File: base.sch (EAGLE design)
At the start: 1 part, among them U1 XC7K160TFBG484

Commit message: adding DRAM.
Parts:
- added J1: AS0A626-U2SN-7F, AS0A626-U2SN-7F:AS0A626-U2SN-7F
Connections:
- removed net N$1: U1B13.VCCO_13@0, U1B13.VCCO_13@1, U1B13.VCCO_13@2, U1B13.VCCO_13@3, U1B13.VCCO_13@4, U1B13.VCCO_13@5
- removed net N$2: U1B0.VCCO_0@0
- removed net N$3: U1B0.VCCO_0@1
- removed net N$4: U1B14.VCCO_14@0, U1B14.VCCO_14@1, U1B14.VCCO_14@2, U1B14.VCCO_14@3, U1B14.VCCO_14@4, U1B14.VCCO_14@5
- removed net N$5: U1B15.VCCO_15@0, U1B15.VCCO_15@1, U1B15.VCCO_15@2, U1B15.VCCO_15@3, U1B15.VCCO_15@4, U1B15.VCCO_15@5
- removed net N$6: U1B16.VCCO_16@0, U1B16.VCCO_16@1, U1B16.VCCO_16@2, U1B16.VCCO_16@3
- removed net N$7: U1B33.VCCO_33@0, U1B33.VCCO_33@1, U1B33.VCCO_33@2, U1B33.VCCO_33@3, U1B33.VCCO_33@4, U1B33.VCCO_33@5
- removed net N$8: U1B34.VCCO_34@0, U1B34.VCCO_34@1, U1B34.VCCO_34@2, U1B34.VCCO_34@3, U1B34.VCCO_34@4, U1B34.VCCO_34@5
- new net VADJ_FPGA: U1B13.VCCO_13@0, U1B13.VCCO_13@1, U1B13.VCCO_13@2, U1B13.VCCO_13@3, U1B13.VCCO_13@4, U1B13.VCCO_13@5, U1B16.VCCO_16@0, U1B16.VCCO_16@1, U1B16.VCCO_16@2, U1B16.VCCO_16@3
- new net VCC1V5_FPGA: U1B33.VCCO_33@0, U1B33.VCCO_33@1, U1B33.VCCO_33@2, U1B33.VCCO_33@3, U1B33.VCCO_33@4, U1B33.VCCO_33@5, U1B34.VCCO_34@0, U1B34.VCCO_34@1, U1B34.VCCO_34@2, U1B34.VCCO_34@3, U1B34.VCCO_34@4, U1B34.VCCO_34@5
- net VCC2V5_FPGA: now also U1B0.VCCO_0@0, U1B0.VCCO_0@1, U1B14.VCCO_14@0, U1B14.VCCO_14@1, U1B14.VCCO_14@2, U1B14.VCCO_14@3, U1B14.VCCO_14@4, U1B14.VCCO_14@5, U1B15.VCCO_15@0, U1B15.VCCO_15@1, U1B15.VCCO_15@2, U1B15.VCCO_15@3, U1B15.VCCO_15@4, U1B15.VCCO_15@5

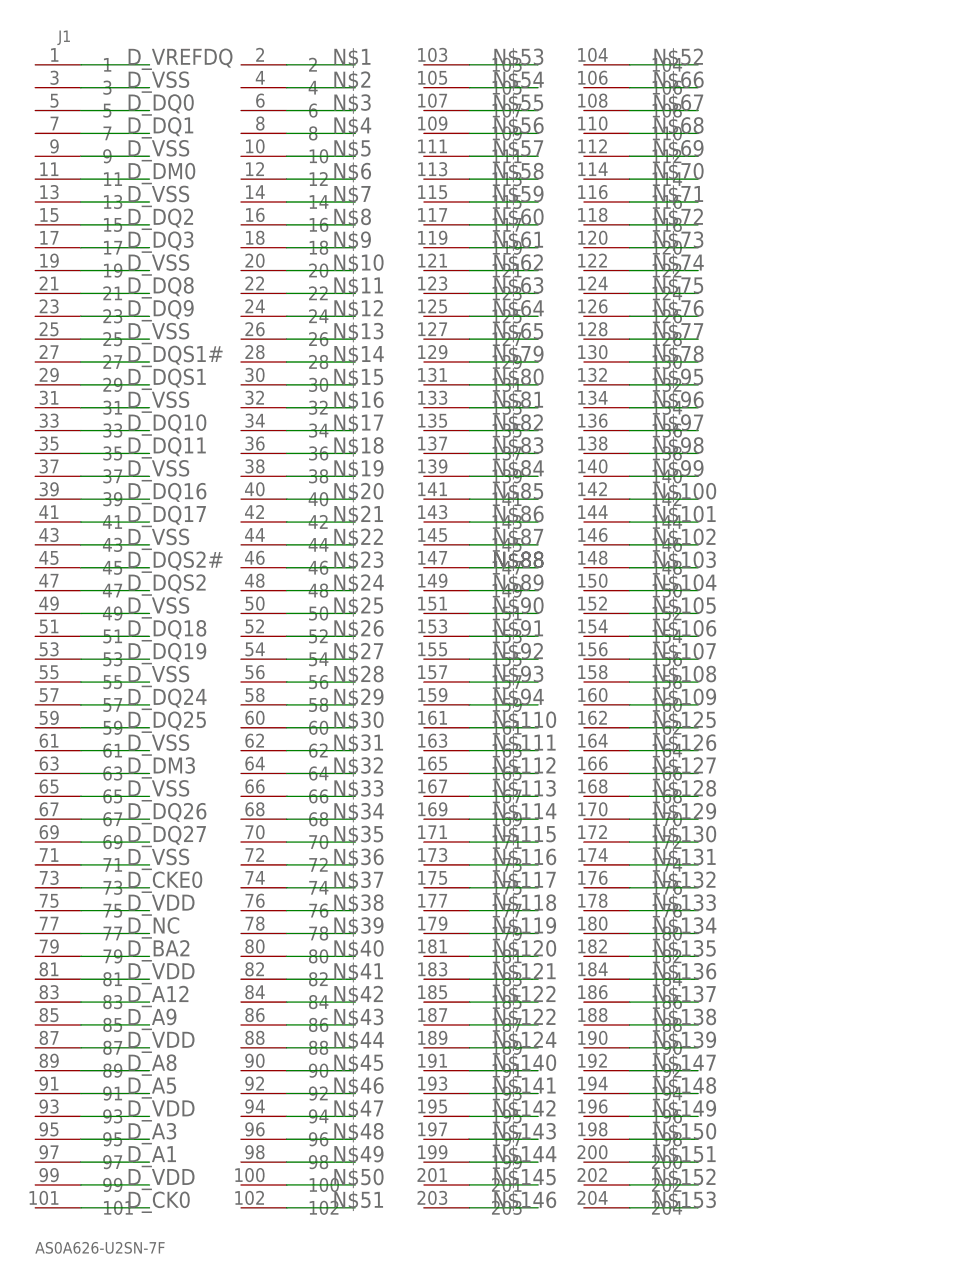
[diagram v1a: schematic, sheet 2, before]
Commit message: updates to DRAM.
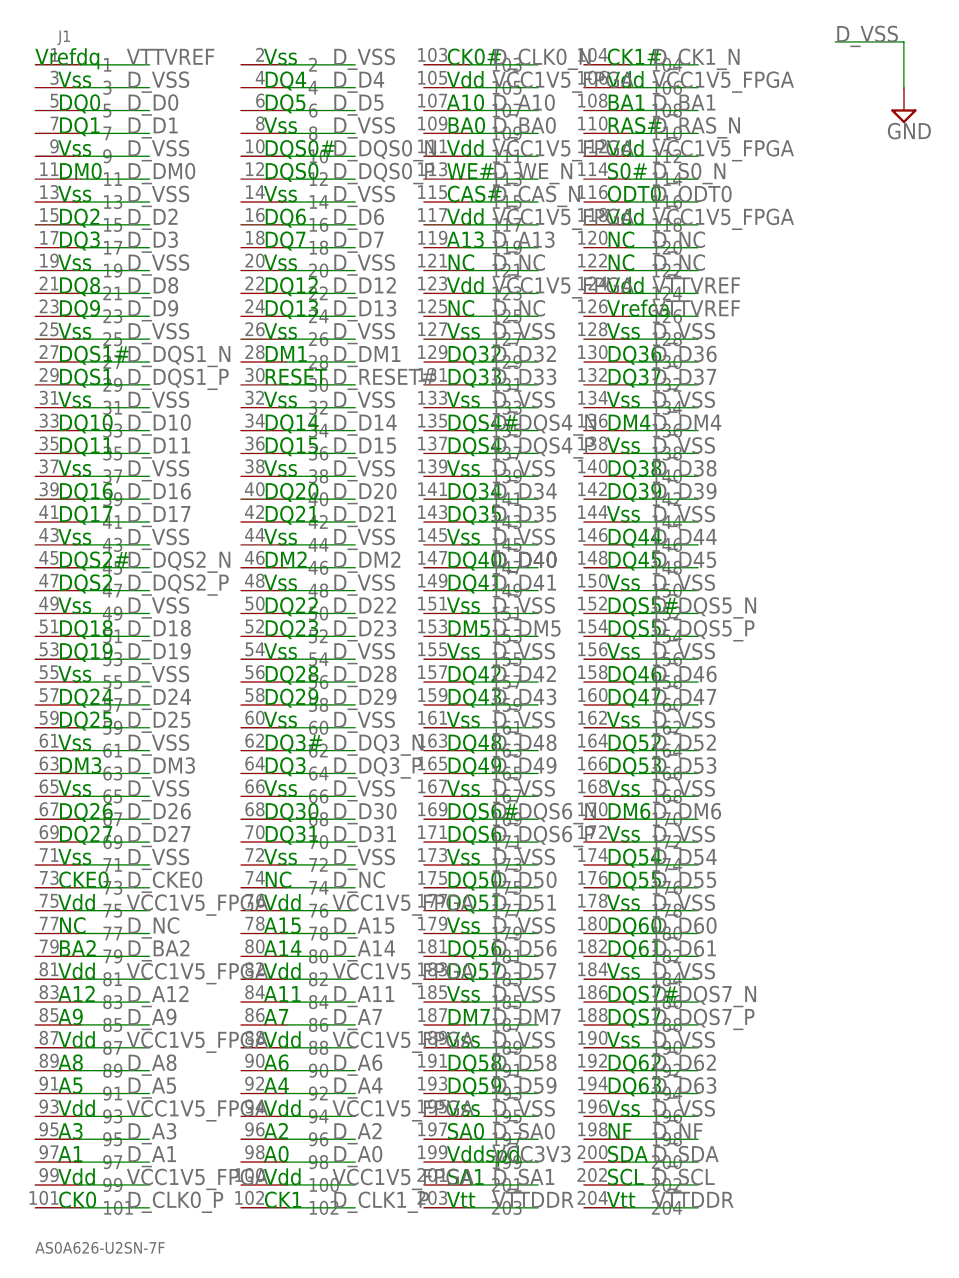
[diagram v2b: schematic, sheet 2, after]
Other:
- note added: "A0"
- note added: "A1"
- note added: "A10"
- note added: "A11"
- note added: "A12"
- note added: "A13"
- note added: "A14"
- note added: "A15"
- note added: "A2"
- note added: "A3"
- note added: "A4"
- note added: "A5"
- note added: "A6"
- note added: "A7"
- note added: "A8"
- note added: "A9"
- note added: "BA0"
- note added: "BA1"
- note added: "BA2"
- note added: "CAS#"
- note added: "CK0"
- note added: "CK0#"
- note added: "CK1"
- note added: "CK1#"
- note added: "CKE0"
- note added: "DM0"
- note added: "DM1"
- note added: "DM2"
- note added: "DM3"
- note added: "DM4"
- note added: "DM5"
- note added: "DM6"
- note added: "DM7"
- note added: "DQ0"
- note added: "DQ1"
- note added: "DQ10"
- note added: "DQ11"
- note added: "DQ12"
- note added: "DQ13"
- note added: "DQ14"
- note added: "DQ15"
- note added: "DQ16"
- note added: "DQ17"
- note added: "DQ18"
- note added: "DQ19"
- note added: "DQ2"
- note added: "DQ20"
- note added: "DQ21"
- note added: "DQ22"
- note added: "DQ23"
- note added: "DQ24"
- note added: "DQ25"
- note added: "DQ26"
- note added: "DQ27"
- note added: "DQ28"
- note added: "DQ29"
- note added: "DQ3"
- note added: "DQ3#"
- note added: "DQ30"
- note added: "DQ31"
- note added: "DQ32"
- note added: "DQ33"
- note added: "DQ34"
- note added: "DQ35"
- note added: "DQ36"
- note added: "DQ37"
- note added: "DQ38"
- note added: "DQ39"
- note added: "DQ4"
- note added: "DQ40"
- note added: "DQ41"
- note added: "DQ42"
- note added: "DQ43"
- note added: "DQ44"
- note added: "DQ45"
- note added: "DQ46"
- note added: "DQ47"
- note added: "DQ48"
- note added: "DQ49"
- note added: "DQ5"
- note added: "DQ50"
- note added: "DQ51"
- note added: "DQ52"
- note added: "DQ53"
- note added: "DQ54"
- note added: "DQ55"
- note added: "DQ56"
- note added: "DQ57"
- note added: "DQ58"
- note added: "DQ59"
- note added: "DQ6"
- note added: "DQ60"
- note added: "DQ61"
- note added: "DQ62"
- note added: "DQ63"
- note added: "DQ7"
- note added: "DQ8"
- note added: "DQ9"
- note added: "DQS0"
- note added: "DQS0#"
- note added: "DQS1"
- note added: "DQS1#"
- note added: "DQS2"
- note added: "DQS2#"
- note added: "DQS4"
- note added: "DQS4#"
- note added: "DQS5"
- note added: "DQS5#"
- note added: "DQS6"
- note added: "DQS6#"
- note added: "DQS7"
- note added: "DQS7#"
- note added: "NC"
- note added: "NF"
- note added: "ODT0"
- note added: "RAS#"
- note added: "RESET"
- note added: "S0#"
- note added: "SA0"
- note added: "SA1"
- note added: "SCL"
- note added: "SDA"
- note added: "Vdd"
- note added: "Vddspd"
- note added: "Vrefca"
- note added: "Vrefdq"
- note added: "Vss"
- note added: "Vtt"
- note added: "WE#"

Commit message: dram wired.
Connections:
- new net D_A0: J1.98, U1B13.IO_L23N_T3_13
- new net D_A1: J1.97, U1B13.IO_L24P_T3_13
- new net D_A10: J1.107, U1B16.IO_L11N_T1_SRCC_16
- new net D_A11: J1.84, U1B16.IO_L12P_T1_MRCC_16
- new net D_A12: J1.83, U1B16.IO_L12N_T1_MRCC_16
- new net D_A13: J1.119, U1B16.IO_L13P_T2_MRCC_16
- new net D_A14: J1.80, U1B16.IO_L13N_T2_MRCC_16
- new net D_A15: J1.78, U1B16.IO_L14P_T2_SRCC_16
- new net D_A2: J1.96, U1B13.IO_L24N_T3_13
- new net D_A3: J1.95, U1B16.IO_L7P_T1_16
- new net D_A4: J1.92, U1B16.IO_L7N_T1_16
- new net D_A5: J1.91, U1B16.IO_L8P_T1_16
- new net D_A6: J1.90, U1B16.IO_L8N_T1_16
- new net D_A7: J1.86, U1B16.IO_L10P_T1_16
- new net D_A8: J1.89, U1B16.IO_L10N_T1_16
- new net D_A9: J1.85, U1B16.IO_L11P_T1_SRCC_16
- new net D_BA0: J1.109, U1B16.IO_L14N_T2_SRCC_16
- new net D_BA1: J1.108, U1B16.IO_L16P_T2_16
- new net D_BA2: J1.79, U1B16.IO_L16N_T2_16
- new net D_CAS_N: J1.115, U1B16.IO_L23N_T3_16
- new net D_CKE0: J1.73, U1B16.IO_L17P_T2_16
- new net D_CLK0_N: J1.103, U1B16.IO_L19P_T3_16
- new net D_CLK0_P: J1.101, U1B16.IO_L20P_T3_16
- new net D_CLK1_N: J1.104, U1B16.IO_L20N_T3_16
- new net D_CLK1_P: J1.102, U1B16.IO_L22P_T3_16
- new net D_D0: J1.5, U1B13.IO_L5N_T0_13
- new net D_D1: J1.7, U1B13.IO_L2P_T0_13
- new net D_D10: J1.33, U1B13.IO_L7N_T1_13
- new net D_D11: J1.35, U1B13.IO_L11P_T1_SRCC_13
- new net D_D12: J1.22, U1B13.IO_L10P_T1_13
- new net D_D13: J1.24, U1B13.IO_L8N_T1_13
- new net D_D14: J1.34, U1B13.IO_L11N_T1_SRCC_13
- new net D_D15: J1.36, U1B33.IO_L15P_T2_DQS_33
- new net D_D16: J1.39, U1B13.IO_L16P_T2_13
- new net D_D17: J1.41, U1B13.IO_L16N_T2_13
- new net D_D18: J1.51, U1B13.IO_L12N_T1_MRCC_13
- new net D_D19: J1.53, U1B13.IO_L13P_T2_MRCC_13
- new net D_D2: J1.15, U1B13.IO_L4N_T0_13
- new net D_D20: J1.40, U1B13.IO_L14N_T2_SRCC_13
- new net D_D21: J1.42, U1B13.IO_L17P_T2_13
- new net D_D22: J1.50, U1B13.IO_L13N_T2_MRCC_13
- new net D_D23: J1.52, U1B13.IO_L14P_T2_SRCC_13
- new net D_D24: J1.57, U1B13.IO_L23P_T3_13
- new net D_D25: J1.59, U1B13.IO_L18P_T2_13
- new net D_D26: J1.67, U1B13.IO_L22P_T3_13
- new net D_D27: J1.69, U1B13.IO_L20P_T3_13
- new net D_D28: J1.56, U1B13.IO_L18N_T2_13
- new net D_D29: J1.58, U1B13.IO_L19P_T3_13
- new net D_D3: J1.17, U1B13.IO_L4P_T0_13
- new net D_D30: J1.68, U1B13.IO_L20N_T3_13
- new net D_D31: J1.70, U1B13.IO_L22N_T3_13
- new net D_D32: J1.129, U1B33.IO_L5P_T0_33
- new net D_D33: J1.131, U1B33.IO_L6P_T0_33
- new net D_D34: J1.141, U1B33.IO_L7N_T1_33
- new net D_D35: J1.143, U1B33.IO_L8P_T1_33
- new net D_D36: J1.130, U1B33.IO_L8N_T1_33
- new net D_D37: J1.132, U1B33.IO_L4P_T0_33
- new net D_D38: J1.140, U1B33.IO_L5N_T0_33
- new net D_D39: J1.142, U1B33.IO_L7P_T1_33
- new net D_D4: J1.4, U1B13.IO_L2N_T0_13
- new net D_D40: J1.147, U1B33.IO_L12N_T1_MRCC_33
- new net D_D41: J1.149, U1B33.IO_L13P_T2_MRCC_33
- new net D_D42: J1.157, U1B33.IO_L11N_T1_SRCC_33
- new net D_D43: J1.159, U1B33.IO_L12P_T1_MRCC_33
- new net D_D44: J1.146, U1B33.IO_L14P_T2_SRCC_33
- new net D_D45: J1.148, U1B33.IO_L13N_T2_MRCC_33
- new net D_D46: J1.158, U1B33.IO_L10N_T1_33
- new net D_D47: J1.160, U1B33.IO_L11P_T1_SRCC_33
- new net D_D48: J1.163, U1B33.IO_L18P_T2_33
- new net D_D49: J1.165, U1B33.IO_L19P_T3_33
- new net D_D5: J1.6, U1B13.IO_L5P_T0_13
- new net D_D50: J1.175, U1B33.IO_L17N_T2_33
- new net D_D51: J1.177, U1B33.IO_L17P_T2_33
- new net D_D52: J1.164, U1B33.IO_L20P_T3_33
- new net D_D53: J1.166, U1B33.IO_L16P_T2_33
- new net D_D54: J1.174, U1B33.IO_L18N_T2_33
- new net D_D55: J1.176, U1B33.IO_L16N_T2_33
- new net D_D56: J1.181, U1B33.IO_L24P_T3_33
- new net D_D57: J1.183, U1B33.IO_L9P_T1_DQS_33
- new net D_D58: J1.191, U1B33.IO_L23P_T3_33
- new net D_D59: J1.193, U1B33.IO_L23N_T3_33
- new net D_D6: J1.16, U1B13.IO_L6P_T0_13
- new net D_D60: J1.180, U1B33.IO_L22P_T3_33
- new net D_D61: J1.182, U1B33.IO_L22N_T3_33
- new net D_D62: J1.192, U1B33.IO_L24N_T3_33
- new net D_D63: J1.194, U1B33.IO_L9N_T1_DQS_33
- new net D_D7: J1.18, U1B13.IO_L1P_T0_13
- new net D_D8: J1.21, U1B13.IO_L8P_T1_13
- new net D_D9: J1.23, U1B13.IO_L10N_T1_13
- new net D_DM0: J1.11, U1B13.IO_L1N_T0_13
- new net D_DM1: J1.28, U1B13.IO_L7P_T1_13
- new net D_DM2: J1.46, U1B13.IO_L12P_T1_MRCC_13
- new net D_DM3: J1.63, U1B13.IO_L17N_T2_13
- new net D_DM4: J1.136, U1B33.IO_L4N_T0_33
- new net D_DM5: J1.153, U1B33.IO_L10P_T1_33
- new net D_DM6: J1.170, U1B33.IO_L14N_T2_SRCC_33
- new net D_DM7: J1.187, U1B33.IO_L20N_T3_33
- new net D_DQS0_N: J1.10, U1B13.IO_L3N_T0_DQS_13
- new net D_DQS0_P: J1.12, U1B13.IO_L3P_T0_DQS_13
- new net D_DQS1_N: J1.27, U1B13.IO_L9N_T1_DQS_13
- new net D_DQS1_P: J1.29, U1B13.IO_L9P_T1_DQS_13
- new net D_DQS2_N: J1.45, U1B13.IO_L15N_T2_DQS_13
- new net D_DQS2_P: J1.47, U1B13.IO_L15P_T2_DQS_13
- new net D_DQS3_N: J1.62, U1B13.IO_L21N_T3_DQS_13
- new net D_DQS3_P: J1.64, U1B13.IO_L21P_T3_DQS_13
- new net D_DQS4_N: J1.135, U1B16.IO_L9N_T1_DQS_16
- new net D_DQS4_P: J1.137, U1B16.IO_L9P_T1_DQS_16
- new net D_DQS5_N: J1.152, U1B16.IO_L15N_T2_DQS_16
- new net D_DQS5_P: J1.154, U1B16.IO_L15P_T2_DQS_16
- new net D_DQS6_N: J1.169, U1B16.IO_L21N_T3_DQS_16
- new net D_DQS6_P: J1.171, U1B16.IO_L21P_T3_DQS_16
- new net D_DQS7_N: J1.186, U1B33.IO_L3P_T0_DQS_33
- new net D_DQS7_P: J1.188, U1B33.IO_L3N_T0_DQS_33
- new net D_NC: J1.120, J1.121, J1.122, J1.125, J1.74, J1.77
- new net D_ODT0: J1.116, U1B33.IO_L2P_T0_33
- new net D_RAS_N: J1.110, U1B16.IO_L23P_T3_16
- new net D_RESET_N: J1.30, U1B33.IO_L15N_T2_DQS_33
- new net D_S0_N: J1.114, U1B33.IO_L1P_T0_33
- new net D_SCL: J1.202
- new net D_SDA: J1.200
- new net D_VSS: J1.127, J1.128, J1.13, J1.133, J1.134, J1.138, J1.139, J1.14, J1.144, J1.145, J1.150, J1.151, J1.155, J1.156, J1.161, J1.162, J1.167, J1.168, J1.172, J1.173, J1.178, J1.179, J1.184, J1.185, J1.189, J1.19, J1.190, J1.195, J1.196, J1.2, J1.20, J1.25, J1.26, J1.3, J1.31, J1.32, J1.37, J1.38, J1.43, J1.44, J1.48, J1.49, J1.54, J1.55, J1.60, J1.61, J1.65, J1.66, J1.71, J1.72, J1.8, J1.9
- new net D_WE_N: J1.113, U1B16.IO_L22N_T3_16
- new net VCC3V3: J1.199
- new net VTTDDR: J1.203, J1.204
- new net VTTVREF: J1.1, J1.124, J1.126, U1B13.IO_L19N_T3_VREF_13, U1B13.IO_L6N_T0_VREF_13, U1B14.IO_L19N_T3_A09_D25_VREF_14, U1B14.IO_L6N_T0_D08_VREF_14, U1B15.IO_L19N_T3_A21_VREF_15, U1B15.IO_L6N_T0_VREF_15, U1B16.IO_6_T0_VREF_16, U1B16.IO_L19N_T3_VREF_16, U1B33.IO_L19N_T3_VREF_33, U1B33.IO_L6N_T0_VREF_33, U1B34.IO_L19N_T3_VREF_34, U1B34.IO_L6N_T0_VREF_34
- net GND: now also J1.197, J1.198, J1.201
- net VCC1V5_FPGA: now also J1.100, J1.105, J1.106, J1.111, J1.112, J1.117, J1.118, J1.123, J1.75, J1.76, J1.81, J1.82, J1.87, J1.88, J1.93, J1.94, J1.99

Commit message: reverting dram, bigger chip.
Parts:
- removed U1: XC7K160TFBG484, xilinx_devices_V6:XC7K160TFBG484
- added U2: XC7K160TFBG676, xilinx_devices_V6:XC7K160TFBG676
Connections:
- removed net FPGA_CCLK: U1B0.CCLK_0
- removed net FPGA_DONE: U1B0.DONE_0
- removed net FPGA_INIT_B: U1B0.INIT_B_0
- removed net FPGA_M0: U1B0.M0_0
- removed net FPGA_M1: U1B0.M1_0
- removed net FPGA_M2: U1B0.M2_0
- removed net FPGA_PROG_B: U1B0.PROGRAM_B_0
- removed net FPGA_TCK_BUF: U1B0.TCK_0
- removed net FPGA_TDI_BUF: U1B0.TDI_0
- removed net FPGA_TMS_BUF: U1B0.TMS_0
- removed net FPGA_VBATT: U1B0.VCCBATT_0
- removed net JTAG_TDO: U1B0.TDO_0
- removed net MGTAVCC: U1BMGTAVCC.MGTAVCC@0, U1BMGTAVCC.MGTAVCC@1, U1BMGTAVCC.MGTAVCC@2, U1BMGTAVCC.MGTAVCC@3
- removed net MGTAVTT: U1BMGTAVTT.MGTAVTT@0, U1BMGTAVTT.MGTAVTT@1, U1BMGTAVTT.MGTAVTT@2, U1BMGTAVTT.MGTAVTT@3
- removed net MGTVCCAUX: U1BMGTVCCAUX.MGTVCCAUX
- removed net VADJ_FPGA: U1B13.VCCO_13@0, U1B13.VCCO_13@1, U1B13.VCCO_13@2, U1B13.VCCO_13@3, U1B13.VCCO_13@4, U1B13.VCCO_13@5, U1B16.VCCO_16@0, U1B16.VCCO_16@1, U1B16.VCCO_16@2, U1B16.VCCO_16@3
- removed net VCC2V5_FPGA: U1B0.CFGBVS_0, U1B0.VCCO_0@0, U1B0.VCCO_0@1, U1B14.VCCO_14@0, U1B14.VCCO_14@1, U1B14.VCCO_14@2, U1B14.VCCO_14@3, U1B14.VCCO_14@4, U1B14.VCCO_14@5, U1B15.VCCO_15@0, U1B15.VCCO_15@1, U1B15.VCCO_15@2, U1B15.VCCO_15@3, U1B15.VCCO_15@4, U1B15.VCCO_15@5
- removed net VCCINT_FPGA: U1BVCCINT.VCCINT@0, U1BVCCINT.VCCINT@1, U1BVCCINT.VCCINT@10, U1BVCCINT.VCCINT@11, U1BVCCINT.VCCINT@12, U1BVCCINT.VCCINT@13, U1BVCCINT.VCCINT@2, U1BVCCINT.VCCINT@3, U1BVCCINT.VCCINT@4, U1BVCCINT.VCCINT@5, U1BVCCINT.VCCINT@6, U1BVCCINT.VCCINT@7, U1BVCCINT.VCCINT@8, U1BVCCINT.VCCINT@9
- removed net VCC_AUX: U1BVCCAUX.VCCAUX@0, U1BVCCAUX.VCCAUX@1, U1BVCCAUX.VCCAUX@2, U1BVCCAUX.VCCAUX@3, U1BVCCAUX.VCCAUX@4, U1BVCCAUX.VCCAUX@5, U1BVCCAUX.VCCAUX@6
- removed net VCC_BRAM: U1BVCCBRAM.VCCBRAM@0, U1BVCCBRAM.VCCBRAM@1, U1BVCCBRAM.VCCBRAM@2
- removed net XADC_AGND: U1BXADC.GNDADC_0, U1BXADC.VREFN_0
- removed net XADC_DXN: U1BTDIODE.DXN_0
- removed net XADC_DXP: U1BTDIODE.DXP_0
- removed net XADC_VCC: U1BXADC.VCCADC_0
- removed net XADC_VN_R: U1BXADC.VN_0
- removed net XADC_VP_R: U1BXADC.VP_0
- removed net XADC_VREFP: U1BXADC.VREFP_0
- new net F_CCLK: U2B0.CCLK_0
- new net F_DONE: U2B0.DONE_0
- new net F_INIT_N: U2B0.INIT_B_0
- new net F_M0: U2B0.M0_0
- new net F_M1: U2B0.M1_0
- new net F_M2: U2B0.M2_0
- new net F_PROG_N: U2B0.PROGRAM_B_0
- new net F_TCK_BUF: U2B0.TCK_0
- new net F_TDI_BUF: U2B0.TDI_0
- new net F_TDO: U2B0.TDO_0
- new net F_TMS_BUF: U2B0.TMS_0
- new net F_VBATT: U2B0.VCCBATT_0
- new net VADJ_F: U2B12.VCCO_12@0, U2B12.VCCO_12@1, U2B12.VCCO_12@2, U2B12.VCCO_12@3, U2B12.VCCO_12@4, U2B12.VCCO_12@5, U2B12.VCCO_12@6, U2B13.VCCO_13@0, U2B13.VCCO_13@1, U2B13.VCCO_13@2, U2B13.VCCO_13@3, U2B13.VCCO_13@4, U2B13.VCCO_13@5, U2B16.VCCO_16@0, U2B16.VCCO_16@1, U2B16.VCCO_16@2, U2B16.VCCO_16@3, U2B16.VCCO_16@4, U2B16.VCCO_16@5, U2B16.VCCO_16@6
- new net VCC1V5_F: U2B32.VCCO_32@0, U2B32.VCCO_32@1, U2B32.VCCO_32@2, U2B32.VCCO_32@3, U2B32.VCCO_32@4, U2B32.VCCO_32@5, U2B33.VCCO_33@0, U2B33.VCCO_33@1, U2B33.VCCO_33@2, U2B33.VCCO_33@3, U2B33.VCCO_33@4, U2B33.VCCO_33@5, U2B34.VCCO_34@0, U2B34.VCCO_34@1, U2B34.VCCO_34@2, U2B34.VCCO_34@3, U2B34.VCCO_34@4, U2B34.VCCO_34@5
- new net VCC2V5_F: U2B0.CFGBVS_0, U2B0.VCCO_0@0, U2B0.VCCO_0@1, U2B14.VCCO_14@0, U2B14.VCCO_14@1, U2B14.VCCO_14@2, U2B14.VCCO_14@3, U2B14.VCCO_14@4, U2B14.VCCO_14@5, U2B15.VCCO_15@0, U2B15.VCCO_15@1, U2B15.VCCO_15@2, U2B15.VCCO_15@3, U2B15.VCCO_15@4, U2B15.VCCO_15@5
- net D_A0: no longer U1B13.IO_L23N_T3_13
- net D_A1: no longer U1B13.IO_L24P_T3_13
- net D_A10: no longer U1B16.IO_L11N_T1_SRCC_16
- net D_A11: no longer U1B16.IO_L12P_T1_MRCC_16
- net D_A12: no longer U1B16.IO_L12N_T1_MRCC_16
- net D_A13: no longer U1B16.IO_L13P_T2_MRCC_16
- net D_A14: no longer U1B16.IO_L13N_T2_MRCC_16
- net D_A15: no longer U1B16.IO_L14P_T2_SRCC_16
- net D_A2: no longer U1B13.IO_L24N_T3_13
- net D_A3: no longer U1B16.IO_L7P_T1_16
- net D_A4: no longer U1B16.IO_L7N_T1_16
- net D_A5: no longer U1B16.IO_L8P_T1_16
- net D_A6: no longer U1B16.IO_L8N_T1_16
- net D_A7: no longer U1B16.IO_L10P_T1_16
- net D_A8: no longer U1B16.IO_L10N_T1_16
- net D_A9: no longer U1B16.IO_L11P_T1_SRCC_16
- net D_BA0: no longer U1B16.IO_L14N_T2_SRCC_16
- net D_BA1: no longer U1B16.IO_L16P_T2_16
- net D_BA2: no longer U1B16.IO_L16N_T2_16
- net D_CAS_N: no longer U1B16.IO_L23N_T3_16
- net D_CKE0: no longer U1B16.IO_L17P_T2_16
- net D_CLK0_N: no longer U1B16.IO_L19P_T3_16
- net D_CLK0_P: no longer U1B16.IO_L20P_T3_16
- net D_CLK1_N: no longer U1B16.IO_L20N_T3_16
- net D_CLK1_P: no longer U1B16.IO_L22P_T3_16
- net D_D0: no longer U1B13.IO_L5N_T0_13
- net D_D1: no longer U1B13.IO_L2P_T0_13
- net D_D10: no longer U1B13.IO_L7N_T1_13
- net D_D11: no longer U1B13.IO_L11P_T1_SRCC_13
- net D_D12: no longer U1B13.IO_L10P_T1_13
- net D_D13: no longer U1B13.IO_L8N_T1_13
- net D_D14: no longer U1B13.IO_L11N_T1_SRCC_13
- net D_D15: no longer U1B33.IO_L15P_T2_DQS_33
- net D_D16: no longer U1B13.IO_L16P_T2_13
- net D_D17: no longer U1B13.IO_L16N_T2_13
- net D_D18: no longer U1B13.IO_L12N_T1_MRCC_13
- net D_D19: no longer U1B13.IO_L13P_T2_MRCC_13
- net D_D2: no longer U1B13.IO_L4N_T0_13
- net D_D20: no longer U1B13.IO_L14N_T2_SRCC_13
- net D_D21: no longer U1B13.IO_L17P_T2_13
- net D_D22: no longer U1B13.IO_L13N_T2_MRCC_13
- net D_D23: no longer U1B13.IO_L14P_T2_SRCC_13
- net D_D24: no longer U1B13.IO_L23P_T3_13
- net D_D25: no longer U1B13.IO_L18P_T2_13
- net D_D26: no longer U1B13.IO_L22P_T3_13
- net D_D27: no longer U1B13.IO_L20P_T3_13
- net D_D28: no longer U1B13.IO_L18N_T2_13
- net D_D29: no longer U1B13.IO_L19P_T3_13
- net D_D3: no longer U1B13.IO_L4P_T0_13
- net D_D30: no longer U1B13.IO_L20N_T3_13
- net D_D31: no longer U1B13.IO_L22N_T3_13
- net D_D32: no longer U1B33.IO_L5P_T0_33
- net D_D33: no longer U1B33.IO_L6P_T0_33
- net D_D34: no longer U1B33.IO_L7N_T1_33
- net D_D35: no longer U1B33.IO_L8P_T1_33
- net D_D36: no longer U1B33.IO_L8N_T1_33
- net D_D37: no longer U1B33.IO_L4P_T0_33
- net D_D38: no longer U1B33.IO_L5N_T0_33
- net D_D39: no longer U1B33.IO_L7P_T1_33
- net D_D4: no longer U1B13.IO_L2N_T0_13
- net D_D40: no longer U1B33.IO_L12N_T1_MRCC_33
- net D_D41: no longer U1B33.IO_L13P_T2_MRCC_33
- net D_D42: no longer U1B33.IO_L11N_T1_SRCC_33
- net D_D43: no longer U1B33.IO_L12P_T1_MRCC_33
- net D_D44: no longer U1B33.IO_L14P_T2_SRCC_33
- net D_D45: no longer U1B33.IO_L13N_T2_MRCC_33
- net D_D46: no longer U1B33.IO_L10N_T1_33
- net D_D47: no longer U1B33.IO_L11P_T1_SRCC_33
- net D_D48: no longer U1B33.IO_L18P_T2_33
- net D_D49: no longer U1B33.IO_L19P_T3_33
- net D_D5: no longer U1B13.IO_L5P_T0_13
- net D_D50: no longer U1B33.IO_L17N_T2_33
- net D_D51: no longer U1B33.IO_L17P_T2_33
- net D_D52: no longer U1B33.IO_L20P_T3_33
- net D_D53: no longer U1B33.IO_L16P_T2_33
- net D_D54: no longer U1B33.IO_L18N_T2_33
- net D_D55: no longer U1B33.IO_L16N_T2_33
- net D_D56: no longer U1B33.IO_L24P_T3_33
- net D_D57: no longer U1B33.IO_L9P_T1_DQS_33
- net D_D58: no longer U1B33.IO_L23P_T3_33
- net D_D59: no longer U1B33.IO_L23N_T3_33
- net D_D6: no longer U1B13.IO_L6P_T0_13
- net D_D60: no longer U1B33.IO_L22P_T3_33
- net D_D61: no longer U1B33.IO_L22N_T3_33
- net D_D62: no longer U1B33.IO_L24N_T3_33
- net D_D63: no longer U1B33.IO_L9N_T1_DQS_33
- net D_D7: no longer U1B13.IO_L1P_T0_13
- net D_D8: no longer U1B13.IO_L8P_T1_13
- net D_D9: no longer U1B13.IO_L10N_T1_13
- net D_DM0: no longer U1B13.IO_L1N_T0_13
- net D_DM1: no longer U1B13.IO_L7P_T1_13
- net D_DM2: no longer U1B13.IO_L12P_T1_MRCC_13
- net D_DM3: no longer U1B13.IO_L17N_T2_13
- net D_DM4: no longer U1B33.IO_L4N_T0_33
- net D_DM5: no longer U1B33.IO_L10P_T1_33
- net D_DM6: no longer U1B33.IO_L14N_T2_SRCC_33
- net D_DM7: no longer U1B33.IO_L20N_T3_33
- net D_DQS0_N: no longer U1B13.IO_L3N_T0_DQS_13
- net D_DQS0_P: no longer U1B13.IO_L3P_T0_DQS_13
- net D_DQS1_N: no longer U1B13.IO_L9N_T1_DQS_13
- net D_DQS1_P: no longer U1B13.IO_L9P_T1_DQS_13
- net D_DQS2_N: no longer U1B13.IO_L15N_T2_DQS_13
- net D_DQS2_P: no longer U1B13.IO_L15P_T2_DQS_13
- net D_DQS3_N: no longer U1B13.IO_L21N_T3_DQS_13
- net D_DQS3_P: no longer U1B13.IO_L21P_T3_DQS_13
- net D_DQS4_N: no longer U1B16.IO_L9N_T1_DQS_16
- net D_DQS4_P: no longer U1B16.IO_L9P_T1_DQS_16
- net D_DQS5_N: no longer U1B16.IO_L15N_T2_DQS_16
- net D_DQS5_P: no longer U1B16.IO_L15P_T2_DQS_16
- net D_DQS6_N: no longer U1B16.IO_L21N_T3_DQS_16
- net D_DQS6_P: no longer U1B16.IO_L21P_T3_DQS_16
- net D_DQS7_N: no longer U1B33.IO_L3P_T0_DQS_33
- net D_DQS7_P: no longer U1B33.IO_L3N_T0_DQS_33
- net D_ODT0: no longer U1B33.IO_L2P_T0_33
- net D_RAS_N: no longer U1B16.IO_L23P_T3_16
- net D_RESET_N: no longer U1B33.IO_L15N_T2_DQS_33
- net D_S0_N: no longer U1B33.IO_L1P_T0_33
- net D_WE_N: no longer U1B16.IO_L22N_T3_16
- net GND: now also U2BGNDA.GND@0, U2BGNDA.GND@1, U2BGNDA.GND@10, U2BGNDA.GND@11, U2BGNDA.GND@12, U2BGNDA.GND@13, U2BGNDA.GND@14, U2BGNDA.GND@15, U2BGNDA.GND@16, U2BGNDA.GND@17, U2BGNDA.GND@18, U2BGNDA.GND@19, U2BGNDA.GND@2, U2BGNDA.GND@20, U2BGNDA.GND@21, U2BGNDA.GND@22, U2BGNDA.GND@23, U2BGNDA.GND@24, U2BGNDA.GND@25, U2BGNDA.GND@26, U2BGNDA.GND@27, U2BGNDA.GND@28, U2BGNDA.GND@29, U2BGNDA.GND@3, U2BGNDA.GND@30, U2BGNDA.GND@31, U2BGNDA.GND@32, U2BGNDA.GND@33, U2BGNDA.GND@34, U2BGNDA.GND@35, U2BGNDA.GND@36, U2BGNDA.GND@37, U2BGNDA.GND@38, U2BGNDA.GND@39, U2BGNDA.GND@4, U2BGNDA.GND@5, U2BGNDA.GND@6, U2BGNDA.GND@7, U2BGNDA.GND@8, U2BGNDA.GND@9, U2BGNDB.GND@40, U2BGNDB.GND@41, U2BGNDB.GND@42, U2BGNDB.GND@43, U2BGNDB.GND@44, U2BGNDB.GND@45, U2BGNDB.GND@46, U2BGNDB.GND@47, U2BGNDB.GND@48, U2BGNDB.GND@49, U2BGNDB.GND@50, U2BGNDB.GND@51, U2BGNDB.GND@52, U2BGNDB.GND@53, U2BGNDB.GND@54, U2BGNDB.GND@55, U2BGNDB.GND@56, U2BGNDB.GND@57, U2BGNDB.GND@58, U2BGNDB.GND@59, U2BGNDB.GND@60, U2BGNDB.GND@61, U2BGNDB.GND@62, U2BGNDB.GND@63, U2BGNDB.GND@64, U2BGNDB.GND@65, U2BGNDB.GND@66, U2BGNDB.GND@67, U2BGNDB.GND@68, U2BGNDB.GND@69, U2BGNDB.GND@70, U2BGNDB.GND@71, U2BGNDB.GND@72, U2BGNDB.GND@73, U2BGNDB.GND@74, U2BGNDB.GND@75, U2BGNDB.GND@76, U2BGNDB.GND@77, U2BGNDB.GND@78, U2BGNDB.GND@79, U2BGNDC.GND@100, U2BGNDC.GND@101, U2BGNDC.GND@102, U2BGNDC.GND@103, U2BGNDC.GND@104, U2BGNDC.GND@105, U2BGNDC.GND@106, U2BGNDC.GND@107, U2BGNDC.GND@108, U2BGNDC.GND@109, U2BGNDC.GND@110, U2BGNDC.GND@111, U2BGNDC.GND@112, U2BGNDC.GND@113, U2BGNDC.GND@114, U2BGNDC.GND@115, U2BGNDC.GND@116, U2BGNDC.GND@117, U2BGNDC.GND@118, U2BGNDC.GND@119, U2BGNDC.GND@80, U2BGNDC.GND@81, U2BGNDC.GND@82, U2BGNDC.GND@83, U2BGNDC.GND@84, U2BGNDC.GND@85, U2BGNDC.GND@86, U2BGNDC.GND@87, U2BGNDC.GND@88, U2BGNDC.GND@89, U2BGNDC.GND@90, U2BGNDC.GND@91, U2BGNDC.GND@92, U2BGNDC.GND@93, U2BGNDC.GND@94, U2BGNDC.GND@95, U2BGNDC.GND@96, U2BGNDC.GND@97, U2BGNDC.GND@98, U2BGNDC.GND@99; no longer U1BGNDA.GND@0, U1BGNDA.GND@1, U1BGNDA.GND@10, U1BGNDA.GND@11, U1BGNDA.GND@12, U1BGNDA.GND@13, U1BGNDA.GND@14, U1BGNDA.GND@15, U1BGNDA.GND@16, U1BGNDA.GND@17, U1BGNDA.GND@18, U1BGNDA.GND@19, U1BGNDA.GND@2, U1BGNDA.GND@20, U1BGNDA.GND@21, U1BGNDA.GND@22, U1BGNDA.GND@23, U1BGNDA.GND@24, U1BGNDA.GND@25, U1BGNDA.GND@26, U1BGNDA.GND@27, U1BGNDA.GND@28, U1BGNDA.GND@29, U1BGNDA.GND@3, U1BGNDA.GND@30, U1BGNDA.GND@31, U1BGNDA.GND@32, U1BGNDA.GND@33, U1BGNDA.GND@34, U1BGNDA.GND@35, U1BGNDA.GND@36, U1BGNDA.GND@37, U1BGNDA.GND@38, U1BGNDA.GND@39, U1BGNDA.GND@4, U1BGNDA.GND@40, U1BGNDA.GND@41, U1BGNDA.GND@42, U1BGNDA.GND@43, U1BGNDA.GND@5, U1BGNDA.GND@6, U1BGNDA.GND@7, U1BGNDA.GND@8, U1BGNDA.GND@9, U1BGNDB.GND@44, U1BGNDB.GND@45, U1BGNDB.GND@46, U1BGNDB.GND@47, U1BGNDB.GND@48, U1BGNDB.GND@49, U1BGNDB.GND@50, U1BGNDB.GND@51, U1BGNDB.GND@52, U1BGNDB.GND@53, U1BGNDB.GND@54, U1BGNDB.GND@55, U1BGNDB.GND@56, U1BGNDB.GND@57, U1BGNDB.GND@58, U1BGNDB.GND@59, U1BGNDB.GND@60, U1BGNDB.GND@61, U1BGNDB.GND@62, U1BGNDB.GND@63, U1BGNDB.GND@64, U1BGNDB.GND@65, U1BGNDB.GND@66, U1BGNDB.GND@67, U1BGNDB.GND@68, U1BGNDB.GND@69, U1BGNDB.GND@70, U1BGNDB.GND@71, U1BGNDB.GND@72, U1BGNDB.GND@73, U1BGNDB.GND@74, U1BGNDB.GND@75, U1BGNDB.GND@76, U1BGNDB.GND@77, U1BGNDB.GND@78, U1BGNDB.GND@79, U1BGNDB.GND@80, U1BGNDB.GND@81, U1BGNDB.GND@82, U1BGNDB.GND@83, U1BGNDB.GND@84, U1BGNDB.GND@85, U1BGNDB.GND@86
- net VCC1V5_FPGA: no longer U1B33.VCCO_33@0, U1B33.VCCO_33@1, U1B33.VCCO_33@2, U1B33.VCCO_33@3, U1B33.VCCO_33@4, U1B33.VCCO_33@5, U1B34.VCCO_34@0, U1B34.VCCO_34@1, U1B34.VCCO_34@2, U1B34.VCCO_34@3, U1B34.VCCO_34@4, U1B34.VCCO_34@5
- net VTTVREF: no longer U1B13.IO_L19N_T3_VREF_13, U1B13.IO_L6N_T0_VREF_13, U1B14.IO_L19N_T3_A09_D25_VREF_14, U1B14.IO_L6N_T0_D08_VREF_14, U1B15.IO_L19N_T3_A21_VREF_15, U1B15.IO_L6N_T0_VREF_15, U1B16.IO_6_T0_VREF_16, U1B16.IO_L19N_T3_VREF_16, U1B33.IO_L19N_T3_VREF_33, U1B33.IO_L6N_T0_VREF_33, U1B34.IO_L19N_T3_VREF_34, U1B34.IO_L6N_T0_VREF_34

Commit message: updating for new lib.
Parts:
- added U$1: PCIEX4_SMALL_CARD, con-pcie-x4 short card:PCIEX4_SMALL_CARD
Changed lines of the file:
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@@
 <?xml version="1.0" encoding="utf-8"?>
 <!DOCTYPE eagle SYSTEM "eagle.dtd">
-<eagle version="7.6.0">
+<eagle version="7.7.0">
 <drawing>
 <settings>
@@
 <part name="SUPPLY4" library="supply2" deviceset="GND" device=""/>
 <part name="U2" library="xilinx_devices_V6" deviceset="XC7K160TFBG676" device=""/>
+<part name="U$1" library="con-pcie-x4 short card" deviceset="PCIEX4_SMALL_CARD" device=""/>
 </parts>
 <sheets>
@@
 <instance part="U2" gate="BVCCAUX_IO" x="-25.4" y="-530.86"/>
 <instance part="U2" gate="BVCCBRAM" x="25.4" y="-462.28"/>
+<instance part="U$1" gate="G$1" x="198.12" y="-266.7"/>
 </instances>
 <busses>
